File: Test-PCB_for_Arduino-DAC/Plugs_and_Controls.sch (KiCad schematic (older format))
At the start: 18 parts, among them J201 PWM_FWD, J202 Molex Mini-fit Jr. 39-28-1243, J203 Pinheader Controls, Q201 BC818, U201 STM6600

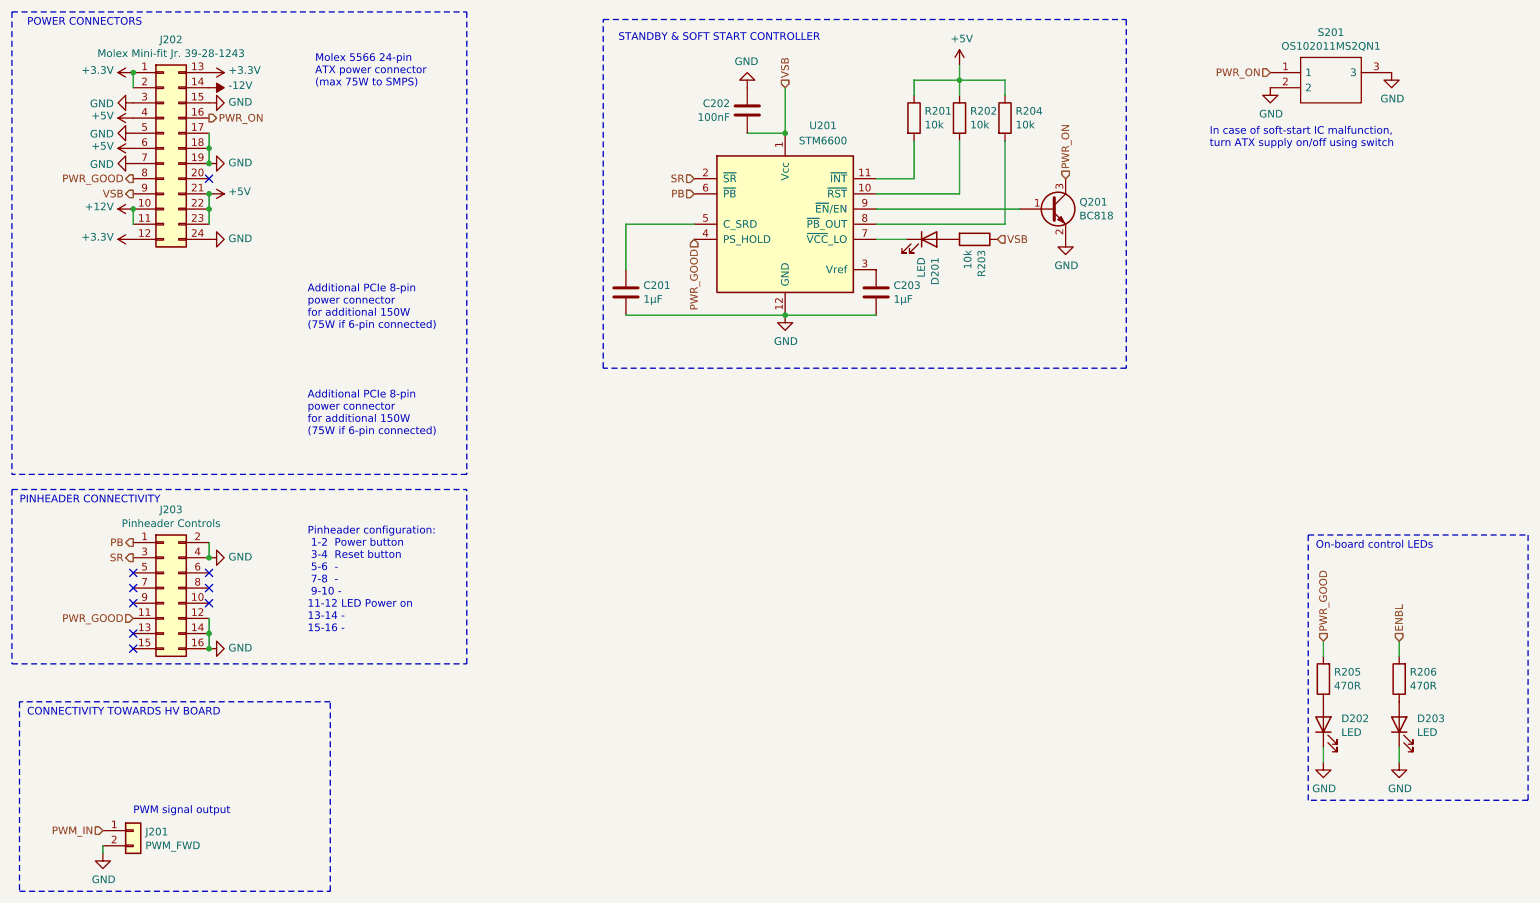
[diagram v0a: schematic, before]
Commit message: Improved Test-PCB Arduino-DAC
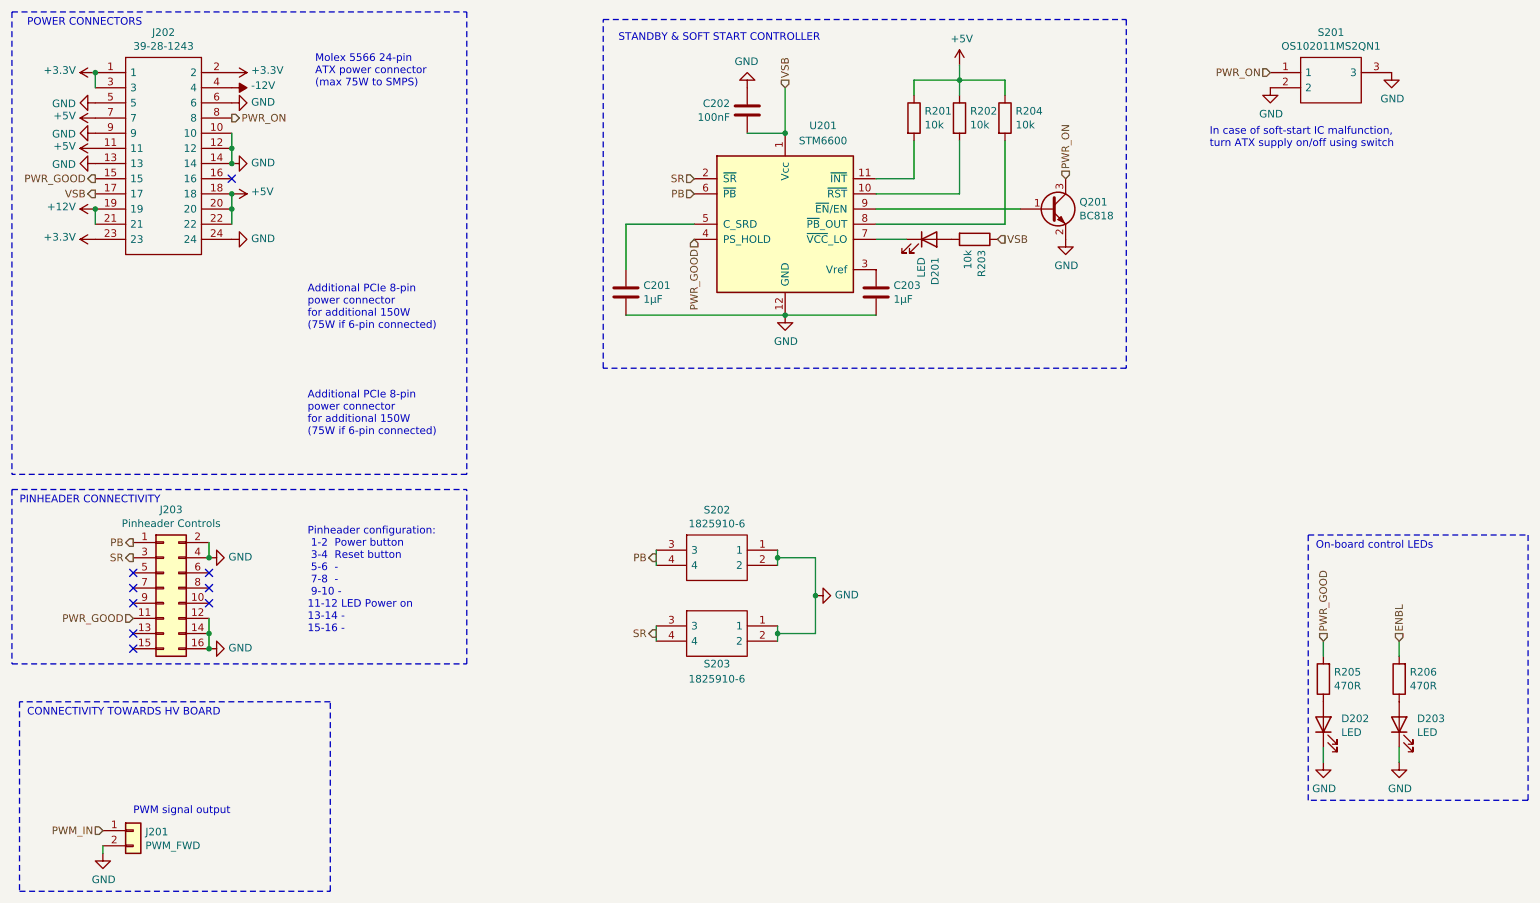
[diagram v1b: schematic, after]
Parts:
- removed J202: Molex Mini-fit Jr. 39-28-1243, Connector_Molex:Molex_Mini-Fit_Jr_5566-24A_2x12_P4.20mm_Vertical, symbol Connector_Generic:Conn_02x12_Top_Bottom
- added J202: 39-28-1243, SamacSys_PCB_library:SHDR24W120P550X420_2X12_5160X960X1310P, symbol SamacSys_lib_loader:39-28-1243
- added S202, S203: 1825910-6, 1825910-6, symbol SamacSys_lib_loader:1825910-6
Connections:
- net +12V: now also J202.19, J202.21
- net +3V3: now also J202.1, J202.2, J202.23, J202.3
- net +5V: now also J202.11, J202.18, J202.20, J202.22, J202.7
- net -12V: now also J202.4
- net GND: now also J202.10, J202.12, J202.13, J202.14, J202.24, J202.5, J202.6, J202.9, S202.1, S202.2, S203.1, S203.2
- net PB: now also S202.3, S202.4
- net PWR_GOOD: now also J202.15
- net PWR_ON: now also J202.8
- net SR: now also S203.3, S203.4
- net VSB: now also J202.17
